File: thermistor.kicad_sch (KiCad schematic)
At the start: 2 parts, among them Q13 AO3400A

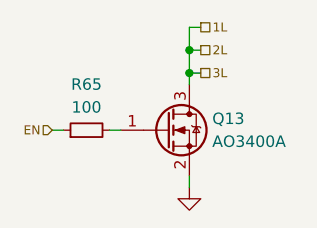
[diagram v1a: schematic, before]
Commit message: *: Use FDV303N for the thermistor MOSFETs
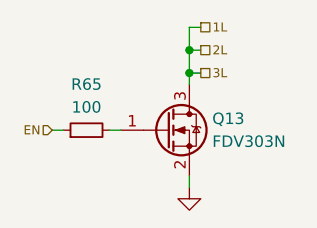
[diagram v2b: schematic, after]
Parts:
- Q13: value AO3400A -> FDV303N; symbol Transistor_FET:AO3400A -> bms:FDV303N; Dist # C347475 -> C80498; Mfr UMW -> onsemi; Mfr # AO3400A -> FDV303N
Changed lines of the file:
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@@
 	)
 	(symbol
-		(lib_id "Transistor_FET:AO3400A")
+		(lib_id "bms:FDV303N")
 		(at 74.93 74.93 0)
 		(unit 1)
@@
 			)
 		)
-		(property "Value" "AO3400A"
+		(property "Value" "FDV303N"
 			(at 80.01 76.2 0)
 			(effects
@@
 			)
 		)
-		(property "Datasheet" "http://www.aosmd.com/pdfs/datasheet/AO3400A.pdf"
+		(property "Datasheet" "https://www.onsemi.com/download/data-sheet/pdf/fdv303n-d.pdf"
 			(at 80.01 78.74 0)
 			(effects
@@
 			)
 		)
-		(property "Description" "30V Vds, 5.7A Id, N-Channel MOSFET, SOT-23"
+		(property "Description" "0.68A Id, 25V Vds, 600mOhm Rds, N-Channel Digital MOSFET, SOT-23, ESD Protected"
 			(at 74.93 74.93 0)
 			(effects
@@
 			)
 		)
-		(property "Dist #" "C347475"
+		(property "Dist #" "C80498"
 			(at 74.93 74.93 0)
 			(effects
@@
 			)
 		)
-		(property "Mfr" "UMW"
+		(property "Mfr" "onsemi"
 			(at 74.93 74.93 0)
 			(effects
@@
 			)
 		)
-		(property "Mfr #" "AO3400A"
+		(property "Mfr #" "FDV303N"
 			(at 74.93 74.93 0)
 			(effects
